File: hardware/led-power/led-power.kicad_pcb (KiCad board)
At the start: 4 copper layers, 86.4 x 86.4 mm, 88 parts, among them J1 String1, J10 Conn_01x05_Male, J11 Qwiic, J12 Qwiic, J16 I2C Header, J17 IRQ, J2 String2, J3 String3, J4 String4, J5 String5, J6 String6, J7 String7, J8 String8, J9 PowerInput, Q1 Q_NMOS_GDS, Q2 Q_NMOS_GDS, Q3 Q_NMOS_GDS, Q4 Q_NMOS_GDS, Q5 Q_NMOS_GDS, Q6 Q_NMOS_GDS, Q7 Q_NMOS_GDS, Q8 Q_NMOS_GDS, Q9 Q_NPN_BEC, U1 MCP6V51, U10 L78L05ACZ-AP, U11 MCP1501, U12 LM317_TO-220, U2 MCP6V51, U3 MCP6V51, U4 MCP6V51, U5 MCP6V51, U6 MCP6V51, U7 MCP6V51, U8 MCP6V51, U9 STM32G030Fx

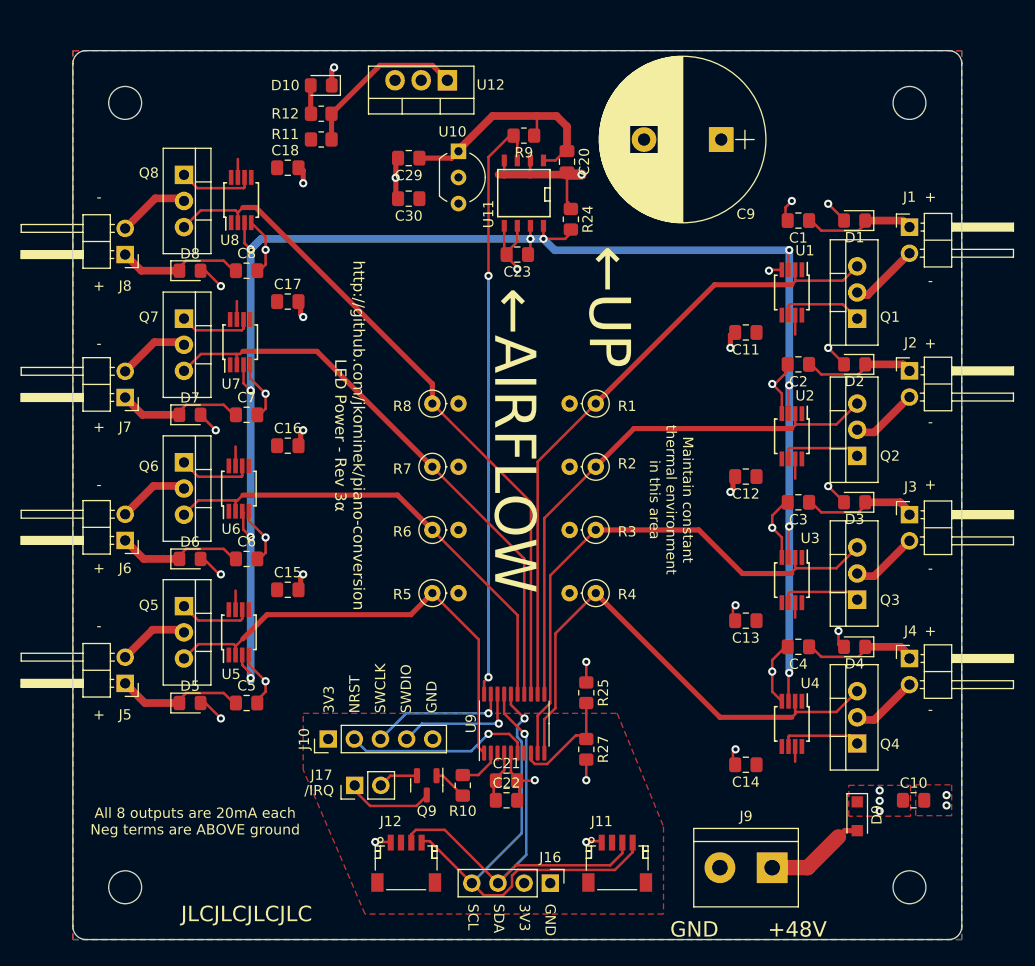
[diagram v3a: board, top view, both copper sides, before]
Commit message: Next revs of the important boards
Includes some tiny DRC tweaks for the LED power board.
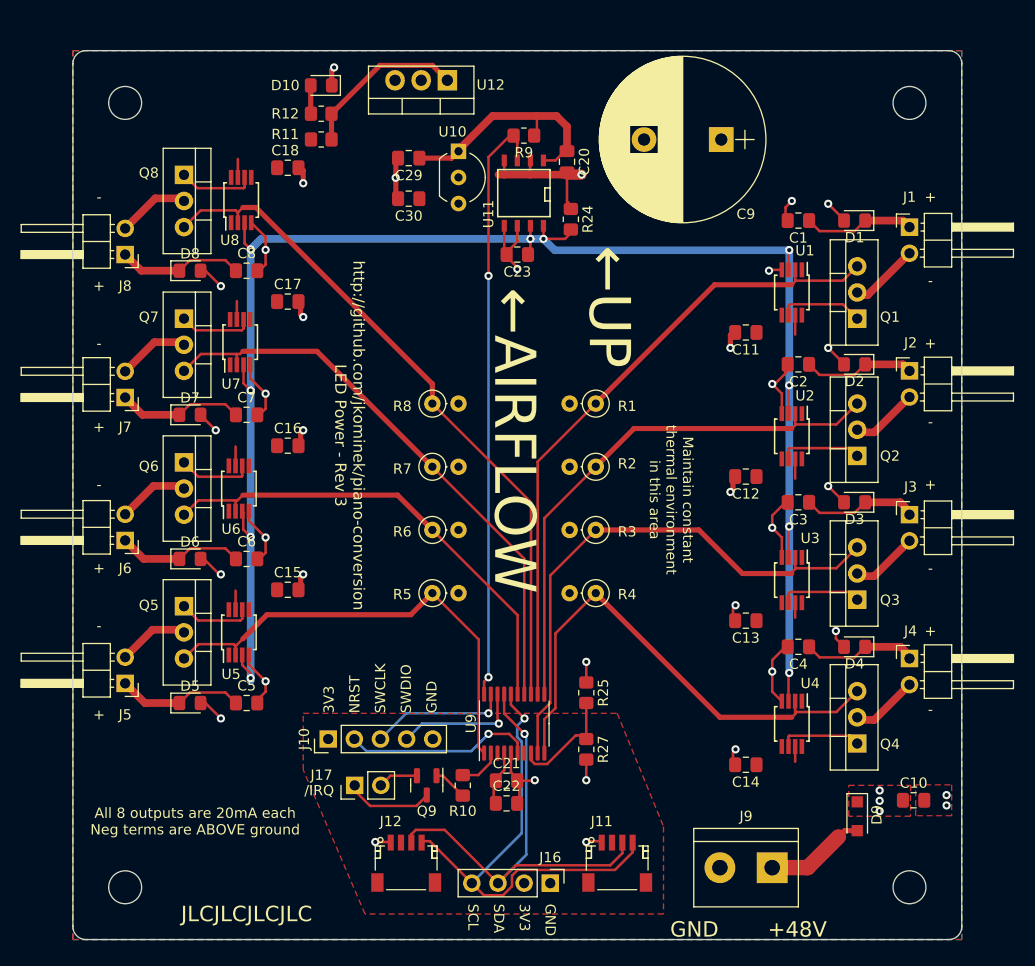
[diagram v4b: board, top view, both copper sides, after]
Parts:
- moved C22 0.30 mm to (113.2, 144.2)
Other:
- board text added: "http://github.com/jkominek/piano-conversion LED Power - Rev 3"
- board text removed: "http://github.com/jkominek/piano-conversion LED Power - Rev 3α"
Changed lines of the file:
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@@
   )
   (footprint "Capacitor_SMD:C_0805_2012Metric_Pad1.18x1.45mm_HandSolder" (layer "F.Cu")
-    (at 113.25 143.9525)
+    (at 113.25 144.25)
     (descr "Capacitor SMD 0805 (2012 Metric), square (rectangular) end terminal, IPC_7351 nominal with elongated pad for handsoldering. (Body size source: IPC-SM-782 page 76, https://www.pcb-3d.com/wordpress/wp-content/uploads/ipc-sm-782a_amendment_1_and_2.pdf, https://docs.google.com/spreadsheets/d/1BsfQQcO9C6DZCsRaXUlFlo91Tg2WpOkGARC1WS5S8t0/edit?usp=sharing), generated with kicad-footprint-generator")
     (tags "capacitor handsolder")
@@
     (effects (font (size 1 1) (thickness 0.15)))
   )
-  (gr_text "http://github.com/jkominek/piano-conversion\nLED Power - Rev 3α" (at 98 108.5 270) (layer "F.SilkS")
+  (gr_text "http://github.com/jkominek/piano-conversion\nLED Power - Rev 3" (at 98 108.5 270) (layer "F.SilkS")
     (effects (font (size 1.1 1.1) (thickness 0.18)))
   )
@@
   (via (at 121 142) (size 0.8) (drill 0.4) (layers "F.Cu" "B.Cu") (net 1))
   (via (at 139.065 103.505) (size 0.8) (drill 0.4) (layers "F.Cu" "B.Cu") (net 1))
-  (segment (start 145.5 128.824) (end 145.716 129.04) (width 0.25) (layer "F.Cu") (net 2))
   (segment (start 83.85 134.5) (end 84 134.5) (width 0.25) (layer "F.Cu") (net 2))
   (segment (start 83.85 106.85) (end 85 108) (width 0.25) (layer "F.Cu") (net 2))
   (segment (start 145.716 101.6) (end 145.716 101.216) (width 0.25) (layer "F.Cu") (net 2))
-  (segment (start 145.5 127.5) (end 145.5 128.824) (width 0.25) (layer "F.Cu") (net 2))
   (segment (start 84 92.5) (end 85.5 94) (width 0.25) (layer "F.Cu") (net 2))
   (segment (start 83.85 134.35) (end 83.85 133.985) (width 0.25) (layer "F.Cu") (net 2))
@@
   (segment (start 85.35 122) (end 83.85 120.5) (width 0.25) (layer "F.Cu") (net 2))
   (segment (start 145.716 87.216) (end 144.5 86) (width 0.25) (layer "F.Cu") (net 2))
+  (segment (start 145.25 128.249) (end 146.041 129.04) (width 0.25) (layer "F.Cu") (net 2))
   (segment (start 83.85 106.5) (end 83.85 106.85) (width 0.25) (layer "F.Cu") (net 2))
   (segment (start 84 134.5) (end 85.5 136) (width 0.25) (layer "F.Cu") (net 2))
@@
   (segment (start 145.716 129.54) (end 145.716 129.216) (width 0.25) (layer "F.Cu") (net 2))
   (segment (start 145.716 115) (end 145.716 114.646) (width 0.25) (layer "F.Cu") (net 2))
+  (segment (start 145.25 127.5) (end 145.25 128.249) (width 0.25) (layer "F.Cu") (net 2))
   (segment (start 85.5 122) (end 85.35 122) (width 0.25) (layer "F.Cu") (net 2))
   (segment (start 83.85 92.5) (end 84 92.5) (width 0.25) (layer "F.Cu") (net 2))
   (via (at 149.5 144) (size 0.8) (drill 0.4) (layers "F.Cu" "B.Cu") (net 2))
   (via (at 149.5 143) (size 0.8) (drill 0.4) (layers "F.Cu" "B.Cu") (net 2))
-  (via (at 145.5 127.5) (size 0.8) (drill 0.4) (layers "F.Cu" "B.Cu") (net 2))
+  (via (at 145.25 127.5) (size 0.8) (drill 0.4) (layers "F.Cu" "B.Cu") (net 2))
   (via (at 144.5 113.43) (size 0.8) (drill 0.4) (layers "F.Cu" "B.Cu") (net 2))
   (via (at 144.5 100) (size 0.8) (drill 0.4) (layers "F.Cu" "B.Cu") (net 2))
@@
   (segment (start 140.705999 90.510001) (end 140.716 90.5) (width 0.75) (layer "B.Cu") (net 20))
   (segment (start 151.765 87.63) (end 152.4 88.265) (width 0.75) (layer "F.Cu") (net 21))
-  (segment (start 147.440999 88.605001) (end 148.416 87.63) (width 0.25) (layer "F.Cu") (net 21))
+  (segment (start 148.091 87.63) (end 147.06648 88.65452) (width 0.25) (layer "F.Cu") (net 21))
+  (segment (start 143.66702 88.65452) (end 142.6425 87.63) (width 0.25) (layer "F.Cu") (net 21))
   (segment (start 148.416 87.63) (end 151.765 87.63) (width 0.75) (layer "F.Cu") (net 21))
-  (segment (start 143.830001 88.605001) (end 147.440999 88.605001) (width 0.25) (layer "F.Cu") (net 21))
-  (segment (start 142.855 87.63) (end 143.830001 88.605001) (width 0.25) (layer "F.Cu") (net 21))
-  (segment (start 142.855 101.6) (end 143.830001 102.575001) (width 0.25) (layer "F.Cu") (net 22))
-  (segment (start 143.830001 102.575001) (end 147.440999 102.575001) (width 0.25) (layer "F.Cu") (net 22))
+  (segment (start 147.06648 88.65452) (end 143.66702 88.65452) (width 0.25) (layer "F.Cu") (net 21))
+  (segment (start 147.06648 102.62452) (end 148.091 101.6) (width 0.25) (layer "F.Cu") (net 22))
+  (segment (start 143.66702 102.62452) (end 147.06648 102.62452) (width 0.25) (layer "F.Cu") (net 22))
   (segment (start 151.765 101.6) (end 152.4 102.235) (width 0.75) (layer "F.Cu") (net 22))
   (segment (start 148.416 101.6) (end 151.765 101.6) (width 0.75) (layer "F.Cu") (net 22))
-  (segment (start 147.440999 102.575001) (end 148.416 101.6) (width 0.25) (layer "F.Cu") (net 22))
+  (segment (start 142.6425 101.6) (end 143.66702 102.62452) (width 0.25) (layer "F.Cu") (net 22))
   (segment (start 151.5 115) (end 148.416 115) (width 0.75) (layer "F.Cu") (net 23))
   (segment (start 152.4 116.205) (end 152.4 115.9) (width 0.75) (layer "F.Cu") (net 23))
-  (segment (start 147.440999 115.975001) (end 143.830001 115.975001) (width 0.25) (layer "F.Cu") (net 23))
-  (segment (start 142.855 115) (end 143.830001 115.975001) (width 0.25) (layer "F.Cu") (net 23))
+  (segment (start 142.6425 115) (end 143.66702 116.02452) (width 0.25) (layer "F.Cu") (net 23))
   (segment (start 152.4 115.9) (end 151.5 115) (width 0.75) (layer "F.Cu") (net 23))
-  (segment (start 148.416 115) (end 147.440999 115.975001) (width 0.25) (layer "F.Cu") (net 23))
-  (segment (start 147.440999 130.015001) (end 148.416 129.04) (width 0.25) (layer "F.Cu") (net 24))
-  (segment (start 143.830001 130.015001) (end 147.440999 130.015001) (width 0.25) (layer "F.Cu") (net 24))
+  (segment (start 143.66702 116.02452) (end 147.06648 116.02452) (width 0.25) (layer "F.Cu") (net 23))
+  (segment (start 147.06648 116.02452) (end 148.091 115) (width 0.25) (layer "F.Cu") (net 23))
+  (segment (start 147.06648 130.06452) (end 143.66702 130.06452) (width 0.25) (layer "F.Cu") (net 24))
+  (segment (start 148.091 129.04) (end 147.06648 130.06452) (width 0.25) (layer "F.Cu") (net 24))
   (segment (start 152.4 130.175) (end 152.4 129.9) (width 0.75) (layer "F.Cu") (net 24))
-  (segment (start 142.855 129.04) (end 143.830001 130.015001) (width 0.25) (layer "F.Cu") (net 24))
   (segment (start 151.54 129.04) (end 148.416 129.04) (width 0.75) (layer "F.Cu") (net 24))
   (segment (start 152.4 129.9) (end 151.54 129.04) (width 0.75) (layer "F.Cu") (net 24))
+  (segment (start 143.66702 130.06452) (end 142.6425 129.04) (width 0.25) (layer "F.Cu") (net 24))
+  (segment (start 85.93798 133.47548) (end 82.49952 133.47548) (width 0.25) (layer "F.Cu") (net 25))
   (segment (start 76.2 132.588) (end 78.112 134.5) (width 0.75) (layer "F.Cu") (net 25))
   (segment (start 78.112 134.5) (end 81.15 134.5) (width 0.75) (layer "F.Cu") (net 25))
-  (segment (start 86.75 134.5) (end 85.775489 133.525489) (width 0.25) (layer "F.Cu") (net 25))
-  (segment (start 85.775489 133.525489) (end 82.124511 133.525489) (width 0.25) (layer "F.Cu") (net 25))
-  (segment (start 82.124511 133.525489) (end 81.15 134.5) (width 0.25) (layer "F.Cu") (net 25))
-  (segment (start 85.774999 119.524999) (end 82.125001 119.524999) (width 0.25) (layer "F.Cu") (net 26))
-  (segment (start 82.125001 119.524999) (end 81.15 120.5) (width 0.25) (layer "F.Cu") (net 26))
+  (segment (start 86.9625 134.5) (end 85.93798 133.47548) (width 0.25) (layer "F.Cu") (net 25))
+  (segment (start 82.49952 133.47548) (end 81.475 134.5) (width 0.25) (layer "F.Cu") (net 25))
+  (segment (start 82.49952 119.47548) (end 81.475 120.5) (width 0.25) (layer "F.Cu") (net 26))
   (segment (start 81.15 120.5) (end 77.997334 120.5) (width 0.75) (layer "F.Cu") (net 26))
+  (segment (start 86.9625 120.5) (end 85.93798 119.47548) (width 0.25) (layer "F.Cu") (net 26))
+  (segment (start 85.93798 119.47548) (end 82.49952 119.47548) (width 0.25) (layer "F.Cu") (net 26))
   (segment (start 77.997334 120.5) (end 76.2 118.702666) (width 0.75) (layer "F.Cu") (net 26))
-  (segment (start 86.75 120.5) (end 85.774999 119.524999) (width 0.25) (layer "F.Cu") (net 26))
   (segment (start 81.15 106.5) (end 77.882667 106.5) (width 0.75) (layer "F.Cu") (net 27))
+  (segment (start 82.49952 105.47548) (end 81.475 106.5) (width 0.25) (layer "F.Cu") (net 27))
   (segment (start 77.882667 106.5) (end 76.2 104.817333) (width 0.75) (layer "F.Cu") (net 27))
-  (segment (start 82.125001 105.524999) (end 81.15 106.5) (width 0.25) (layer "F.Cu") (net 27))
-  (segment (start 86.75 106.5) (end 85.774999 105.524999) (width 0.25) (layer "F.Cu") (net 27))
-  (segment (start 85.774999 105.524999) (end 82.125001 105.524999) (width 0.25) (layer "F.Cu") (net 27))
-  (segment (start 86.75 92.5) (end 85.774999 91.524999) (width 0.25) (layer "F.Cu") (net 28))
-  (segment (start 82.125001 91.524999) (end 81.15 92.5) (width 0.25) (layer "F.Cu") (net 28))
+  (segment (start 85.93798 105.47548) (end 82.49952 105.47548) (width 0.25) (layer "F.Cu") (net 27))
+  (segment (start 86.9625 106.5) (end 85.93798 105.47548) (width 0.25) (layer "F.Cu") (net 27))
+  (segment (start 82.49952 91.47548) (end 81.475 92.5) (width 0.25) (layer "F.Cu") (net 28))
+  (segment (start 85.93798 91.47548) (end 82.49952 91.47548) (width 0.25) (layer "F.Cu") (net 28))
   (segment (start 81.15 92.5) (end 77.768 92.5) (width 0.75) (layer "F.Cu") (net 28))
-  (segment (start 85.774999 91.524999) (end 82.125001 91.524999) (width 0.25) (layer "F.Cu") (net 28))
   (segment (start 77.768 92.5) (end 76.2 90.932) (width 0.75) (layer "F.Cu") (net 28))
+  (segment (start 86.9625 92.5) (end 85.93798 91.47548) (width 0.25) (layer "F.Cu") (net 28))
   (segment (start 139.061 150.495) (end 142.505 150.495) (width 1.5) (layer "F.Cu") (net 29))
   (segment (start 147.32 146.9) (end 146.1 146.9) (width 0.5) (layer "F.Cu") (net 29))
